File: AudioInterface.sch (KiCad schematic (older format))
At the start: 4 parts, among them J3 REM/DATA, U3 HS-100B

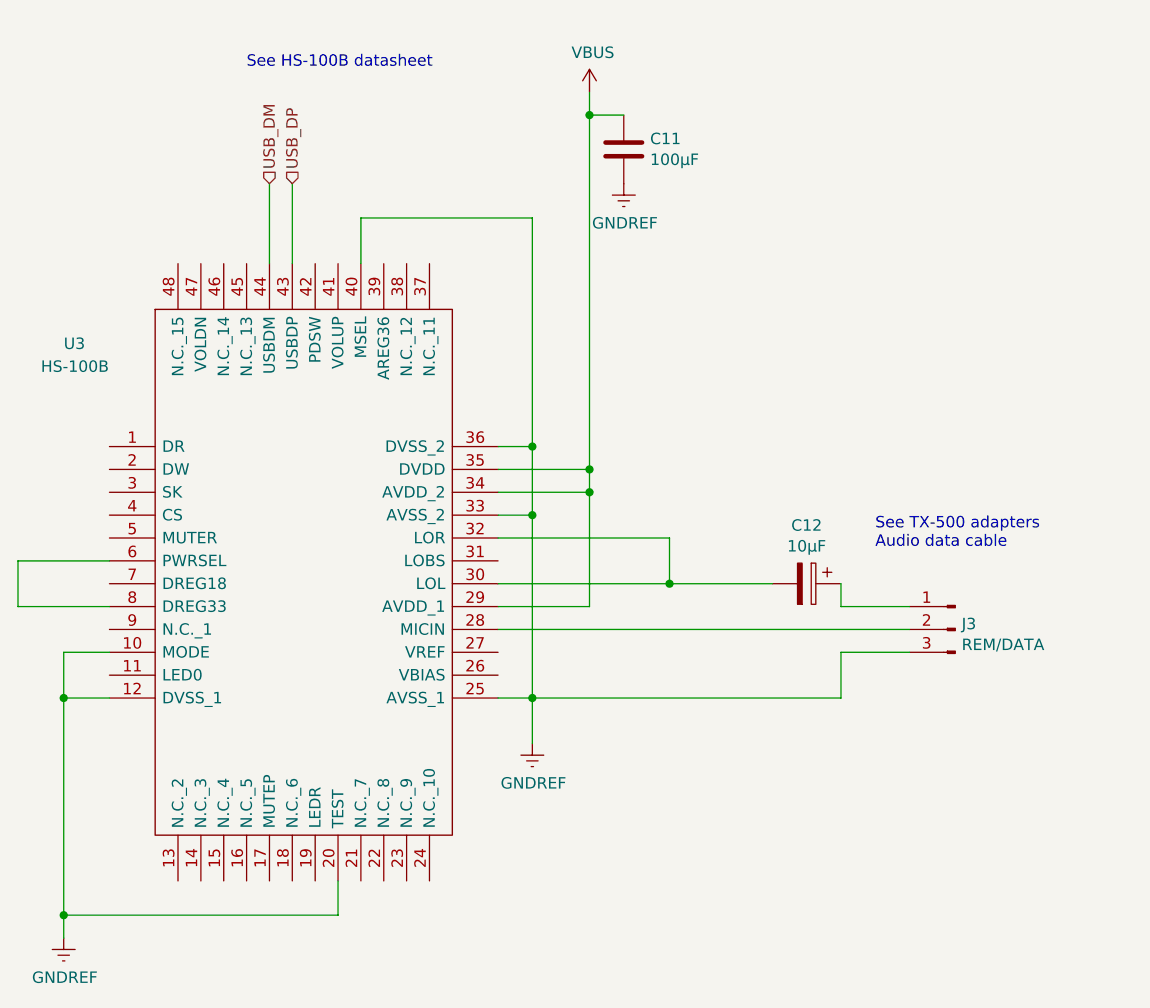
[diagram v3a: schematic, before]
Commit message: First pass at routing PCB
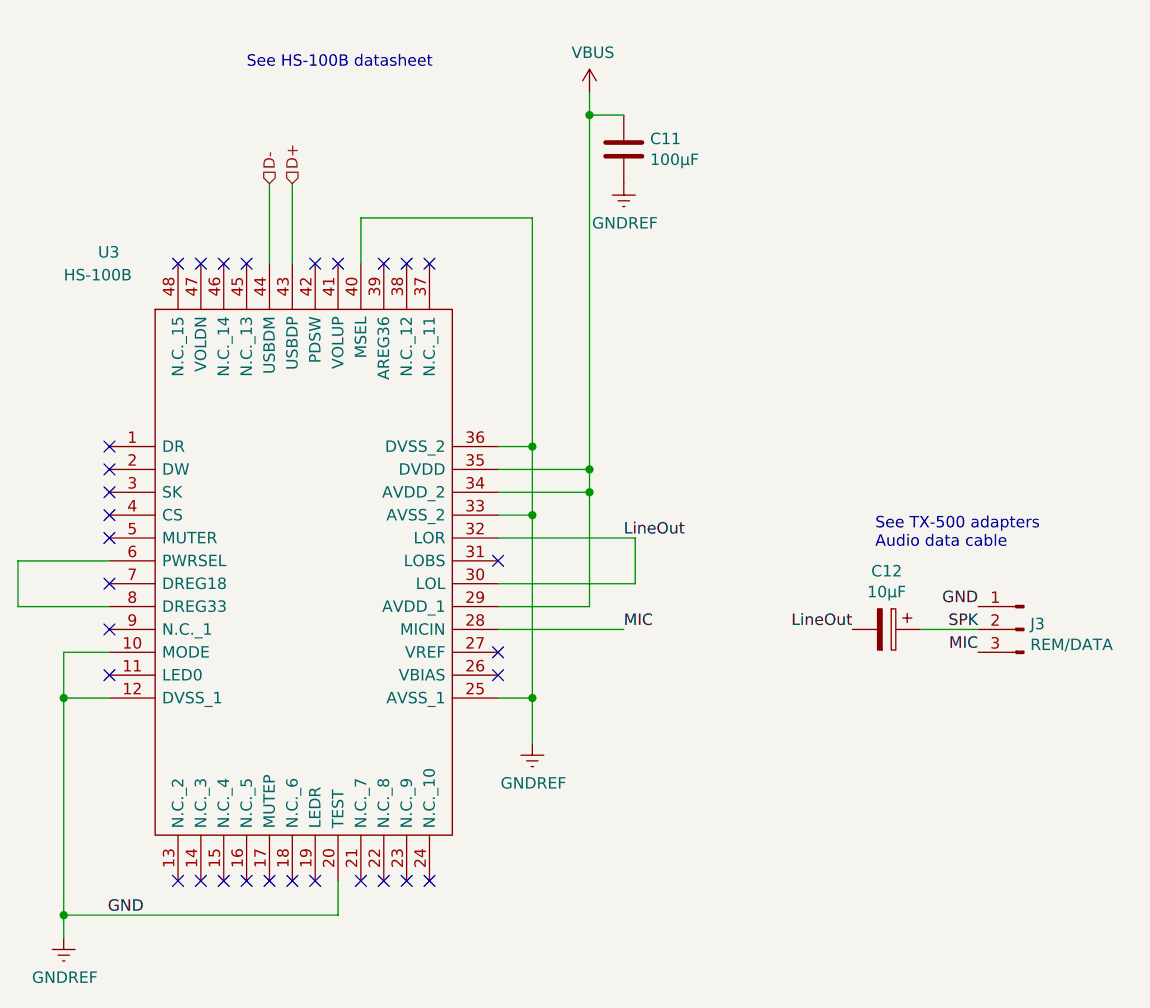
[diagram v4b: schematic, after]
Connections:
- net GNDREF: now also J3.1 (Pin_1); no longer J3.3 (Pin_3)
- net SPK: now reaches C12.1
- net SPK: now also J3.2 (Pin_2); no longer J3.1 (Pin_1)
- net LineOut: now reaches C12.2, U3.30 (LOL), U3.32 (LOR)
- net MIC: now reaches U3.28 (MICIN)
- net MIC: now also J3.3 (Pin_3); no longer J3.2 (Pin_2)
- net USB_DM renamed D-
- net USB_DP renamed D+
- no-connect marks 0 -> 31
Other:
- moved on the sheet: C12, J3
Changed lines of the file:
@@
 $Descr A4 11693 8268
 encoding utf-8
-Sheet 3 6
+Sheet 4 6
 Title "TX-500 Data Interface"
 Date "2021-03-15"
 Rev "0.1"
 Comp "Chris Keller K0SWE"
-Comment1 ""
+Comment1 "Licensed under Apache-2.0"
 Comment2 ""
 Comment3 ""
@@
 AR Path="/605AF753" Ref="IC?"  Part="1"
 AR Path="/605AB33C/605AF753" Ref="U3"  Part="1"
-F 0 "U3" H 4450 3900 50  0000 L CNN
-F 1 "HS-100B" H 4350 3800 50  0000 L CNN
+F 0 "U3" H 4600 4300 50  0000 L CNN
+F 1 "HS-100B" H 4450 4200 50  0000 L CNN
 F 2 "Package_QFP:LQFP-48_7x7mm_P0.5mm" H 6200 4050 50  0001 L CNN
 F 3 "1.6" H 6200 3950 50  0001 L CNN
@@
 L Connector:Conn_01x03_Male J?
 U 1 1 605AF759
-P 8350 4250
+P 8650 4250
 AR Path="/605AF759" Ref="J?"  Part="1"
 AR Path="/605AB33C/605AF759" Ref="J3"  Part="1"
-F 0 "J3" H 8322 4274 50  0000 R CNN
-F 1 "REM/DATA" H 8322 4183 50  0000 R CNN
-F 2 "Connector_JST:JST_PH_B3B-PH-SM4-TB_1x03-1MP_P2.00mm_Vertical" H 8350 4250 50  0001 C CNN
-F 3 "https://www.mouser.com/datasheet/2/737/4389_C13924-001_CCP-W20-03-BK-SMT-R-A-1708610.pdf" H 8350 4250 50  0001 C CNN
-F 4 "TX-500 REM/DATA Interconnect" H 8322 4374 50  0001 C CNN "Description"
-F 5 "JST" H 8322 4374 50  0001 C CNN "Manufacturer_Name"
-F 6 "B3B-PH-SM4-TB" H 8322 4374 50  0001 C CNN "Manufacturer_Part_Number"
-F 7 "0.35" H 8322 4374 50  0001 C CNN "Price"
-F 8 "485-4389" H 8322 4374 50  0001 C CNN "Vendor Part Number"
-F 9 "Mouser" H 8322 4374 50  0001 C CNN "Vendor"
-	1    8350 4250
+F 0 "J3" H 8622 4274 50  0000 R CNN
+F 1 "REM/DATA" H 8622 4183 50  0000 R CNN
+F 2 "Connector_JST:JST_PH_B3B-PH-SM4-TB_1x03-1MP_P2.00mm_Vertical" H 8650 4250 50  0001 C CNN
+F 3 "https://www.mouser.com/datasheet/2/737/4389_C13924-001_CCP-W20-03-BK-SMT-R-A-1708610.pdf" H 8650 4250 50  0001 C CNN
+F 4 "TX-500 REM/DATA Interconnect" H 8622 4374 50  0001 C CNN "Description"
+F 5 "JST" H 8622 4374 50  0001 C CNN "Manufacturer_Name"
+F 6 "B3B-PH-SM4-TB" H 8622 4374 50  0001 C CNN "Manufacturer_Part_Number"
+F 7 "0.35" H 8622 4374 50  0001 C CNN "Price"
+F 8 "485-4389" H 8622 4374 50  0001 C CNN "Vendor Part Number"
+F 9 "Mouser" H 8622 4374 50  0001 C CNN "Vendor"
+	1    8650 4250
 	-1   0    0    -1
 $EndComp
@@
 L Device:CP C12
 U 1 1 604CC1E1
-P 7700 4050
-F 0 "C12" V 7445 4050 50  0000 C CNN
-F 1 "10μF" V 7536 4050 50  0000 C CNN
-F 2 "Capacitor_SMD:C_1210_3225Metric" H 7738 3900 50  0001 C CNN
-F 3 "https://www.mouser.com/datasheet/2/210/WTC_MLCC_General_Purpose-1534899.pdf" H 7700 4050 50  0001 C CNN
-F 4 "Walsin" H 7445 4150 50  0001 C CNN "Manufacturer_Name"
-F 5 "1210F106Z100CT" H 7445 4150 50  0001 C CNN "Manufacturer_Part_Number"
-F 6 "0.29" H 7445 4150 50  0001 C CNN "Price"
-F 7 "791-1210F106Z100CT" H 7445 4150 50  0001 C CNN "Vendor Part Number"
-F 8 "Mouser" H 7445 4150 50  0001 C CNN "Vendor"
-	1    7700 4050
+P 8050 4250
+F 0 "C12" V 7795 4250 50  0000 C CNN
+F 1 "10μF" V 7886 4250 50  0000 C CNN
+F 2 "Capacitor_SMD:C_1210_3225Metric" H 8088 4100 50  0001 C CNN
+F 3 "https://www.mouser.com/datasheet/2/210/WTC_MLCC_General_Purpose-1534899.pdf" H 8050 4250 50  0001 C CNN
+F 4 "Walsin" H 7795 4350 50  0001 C CNN "Manufacturer_Name"
+F 5 "1210F106Z100CT" H 7795 4350 50  0001 C CNN "Manufacturer_Part_Number"
+F 6 "0.29" H 7795 4350 50  0001 C CNN "Price"
+F 7 "791-1210F106Z100CT" H 7795 4350 50  0001 C CNN "Vendor Part Number"
+F 8 "Mouser" H 7795 4350 50  0001 C CNN "Vendor"
+	1    8050 4250
 	0    1    1    0
 $EndComp
@@
 See TX-500 adapters\nAudio data cable
 Text HLabel 5450 2300 1    50   Input ~ 0
-USB_DP
+D+
 Text HLabel 5350 2300 1    50   Input ~ 0
-USB_DM
+D-
 Wire Wire Line
 	6350 3450 6500 3450
@@
 	4650 4550 4450 4550
 Wire Wire Line
-	6350 4050 7100 4050
-Wire Wire Line
-	7100 4050 7100 3850
-Wire Wire Line
-	6350 3850 7100 3850
+	6350 4050 6950 4050
+Wire Wire Line
+	6950 4050 6950 3850
+Wire Wire Line
+	6350 3850 6950 3850
 Wire Wire Line
 	6350 3550 6750 3550
@@
 Connection ~ 6750 2000
 Connection ~ 6750 3550
-Wire Wire Line
-	7850 4050 7850 4150
-Wire Wire Line
-	7850 4150 8150 4150
-Wire Wire Line
-	7850 4550 7850 4350
-Wire Wire Line
-	7850 4350 8150 4350
-Wire Wire Line
-	7100 4050 7550 4050
-Connection ~ 7100 4050
-Wire Wire Line
-	6350 4250 8150 4250
-Wire Wire Line
-	6500 4550 7850 4550
+Text Label 8450 4250 2    50   ~ 0
+SPK
+Text Label 8450 4350 2    50   ~ 0
+MIC
+Text Label 8450 4150 2    50   ~ 0
+GND
+Text Label 6900 4250 0    50   ~ 0
+MIC
+Text Label 4800 5500 2    50   ~ 0
+GND
+Wire Wire Line
+	8200 4250 8450 4250
+Text Label 6900 3850 0    50   ~ 0
+LineOut
+Text Label 7900 4250 2    50   ~ 0
+LineOut
+NoConn ~ 4650 3450
+NoConn ~ 4650 3550
+NoConn ~ 4650 3650
+NoConn ~ 4650 3750
+NoConn ~ 4650 3850
+NoConn ~ 4650 4050
+NoConn ~ 4650 4250
+NoConn ~ 4650 4450
+NoConn ~ 4950 5350
+NoConn ~ 5050 5350
+NoConn ~ 5150 5350
+NoConn ~ 5250 5350
+NoConn ~ 5350 5350
+NoConn ~ 5450 5350
+NoConn ~ 5550 5350
+NoConn ~ 5750 5350
+NoConn ~ 5850 5350
+NoConn ~ 5950 5350
+NoConn ~ 6050 5350
+NoConn ~ 6350 4450
+NoConn ~ 6350 4350
+NoConn ~ 6350 3950
+Wire Wire Line
+	6350 4250 6900 4250
+NoConn ~ 4950 2650
+NoConn ~ 5050 2650
+NoConn ~ 5150 2650
+NoConn ~ 5250 2650
+NoConn ~ 5550 2650
+NoConn ~ 5650 2650
+NoConn ~ 5850 2650
+NoConn ~ 5950 2650
+NoConn ~ 6050 2650
 $EndSCHEMATC
